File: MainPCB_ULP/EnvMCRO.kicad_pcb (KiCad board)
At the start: 2 copper layers, 109.6 x 69.7 mm, 43 parts, among them SW1 Rotary_Encoder_Switch, U1 Pico

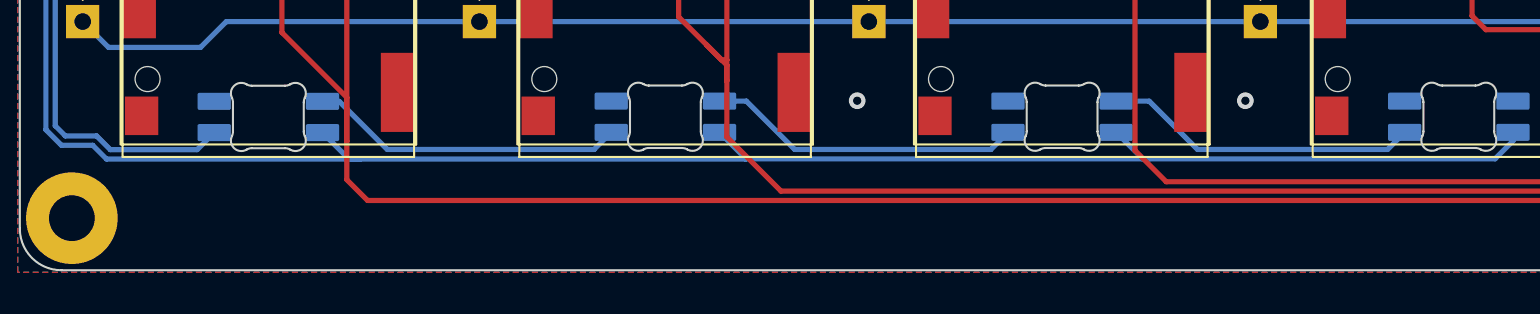
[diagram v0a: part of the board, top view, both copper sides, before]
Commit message: update gitignore
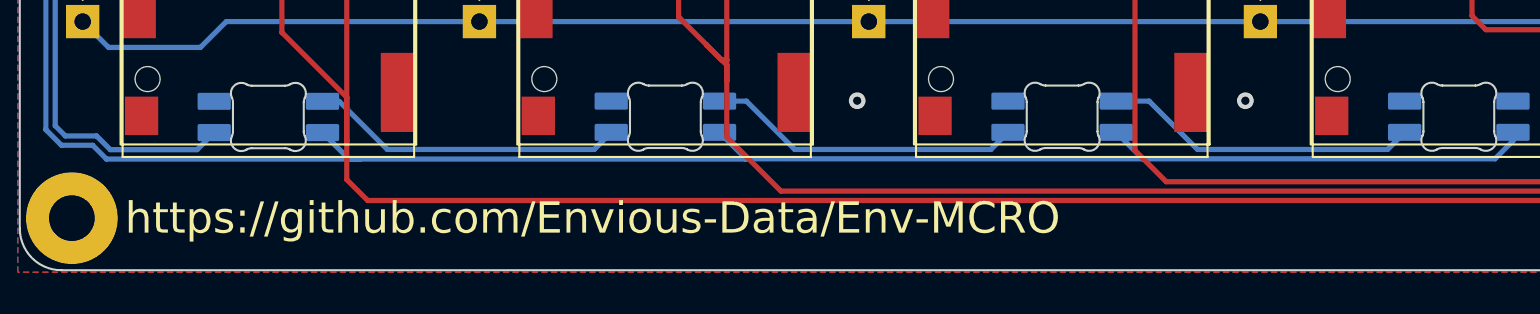
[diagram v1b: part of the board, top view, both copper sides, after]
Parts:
- added kibuzzard-63CB16AC: G***, kibuzzard-63CB16AC, F.Cu at (156.1, 56.0)
- added kibuzzard-63CB16FA: G***, kibuzzard-63CB16FA, F.Cu at (156.1, 54.2)
